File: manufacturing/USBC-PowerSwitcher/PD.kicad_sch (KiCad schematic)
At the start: 23 parts, among them J1 USB_C_Receptacle, J3 VDC, Q1 2N7002K, U2 CYPD3177-24LQXQ

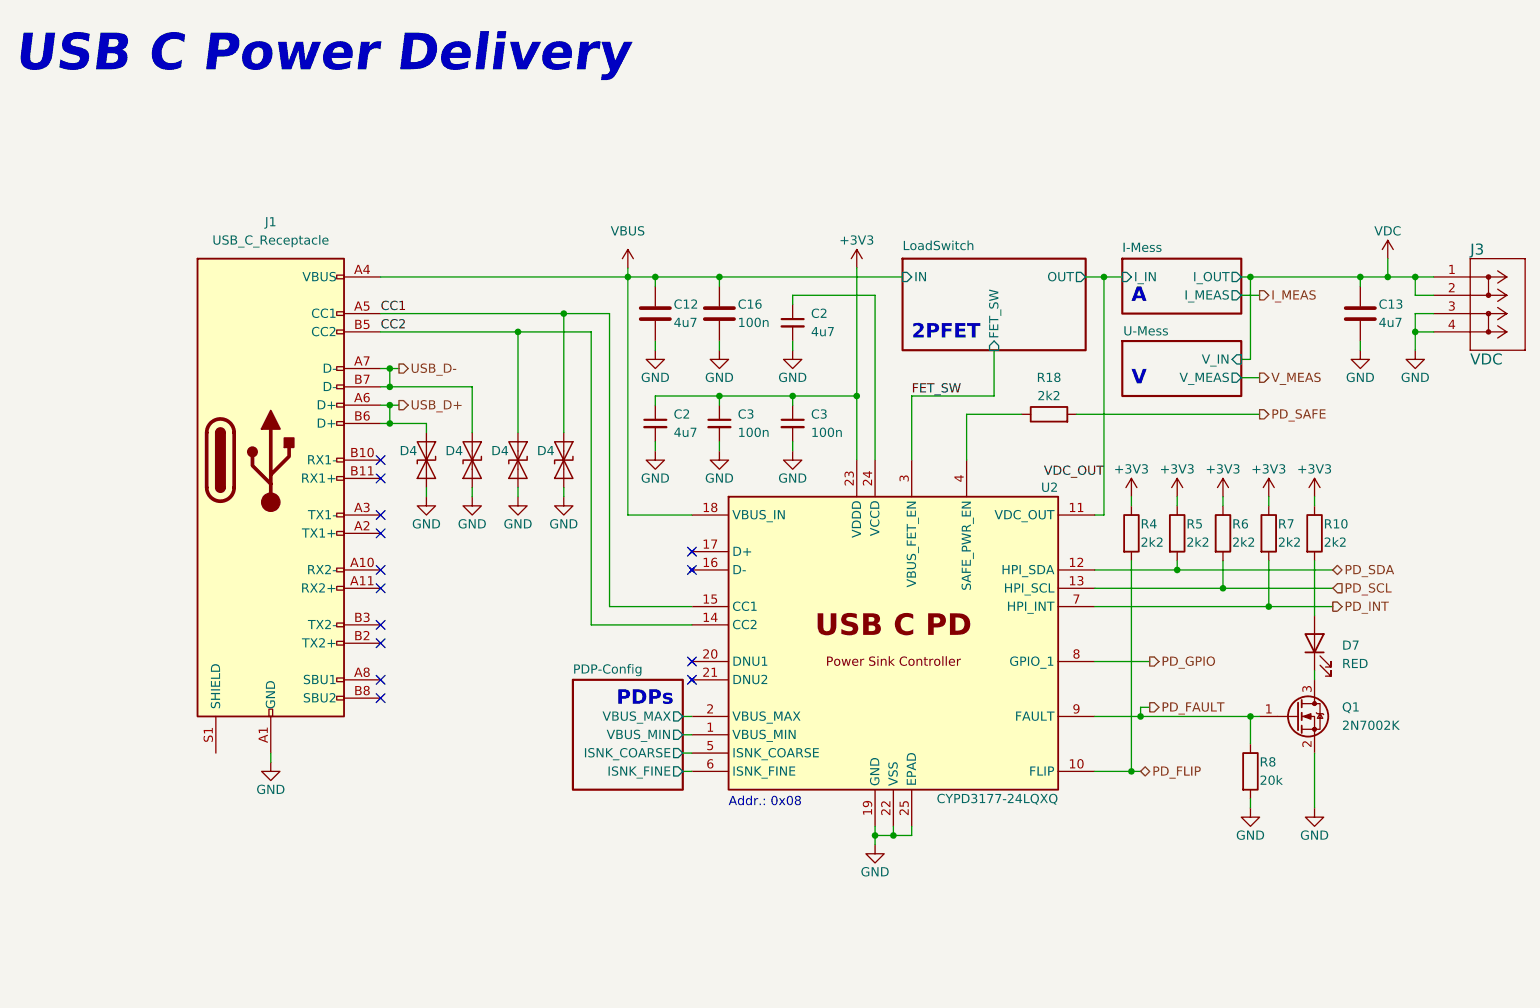
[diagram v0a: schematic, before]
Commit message: First Rough placement
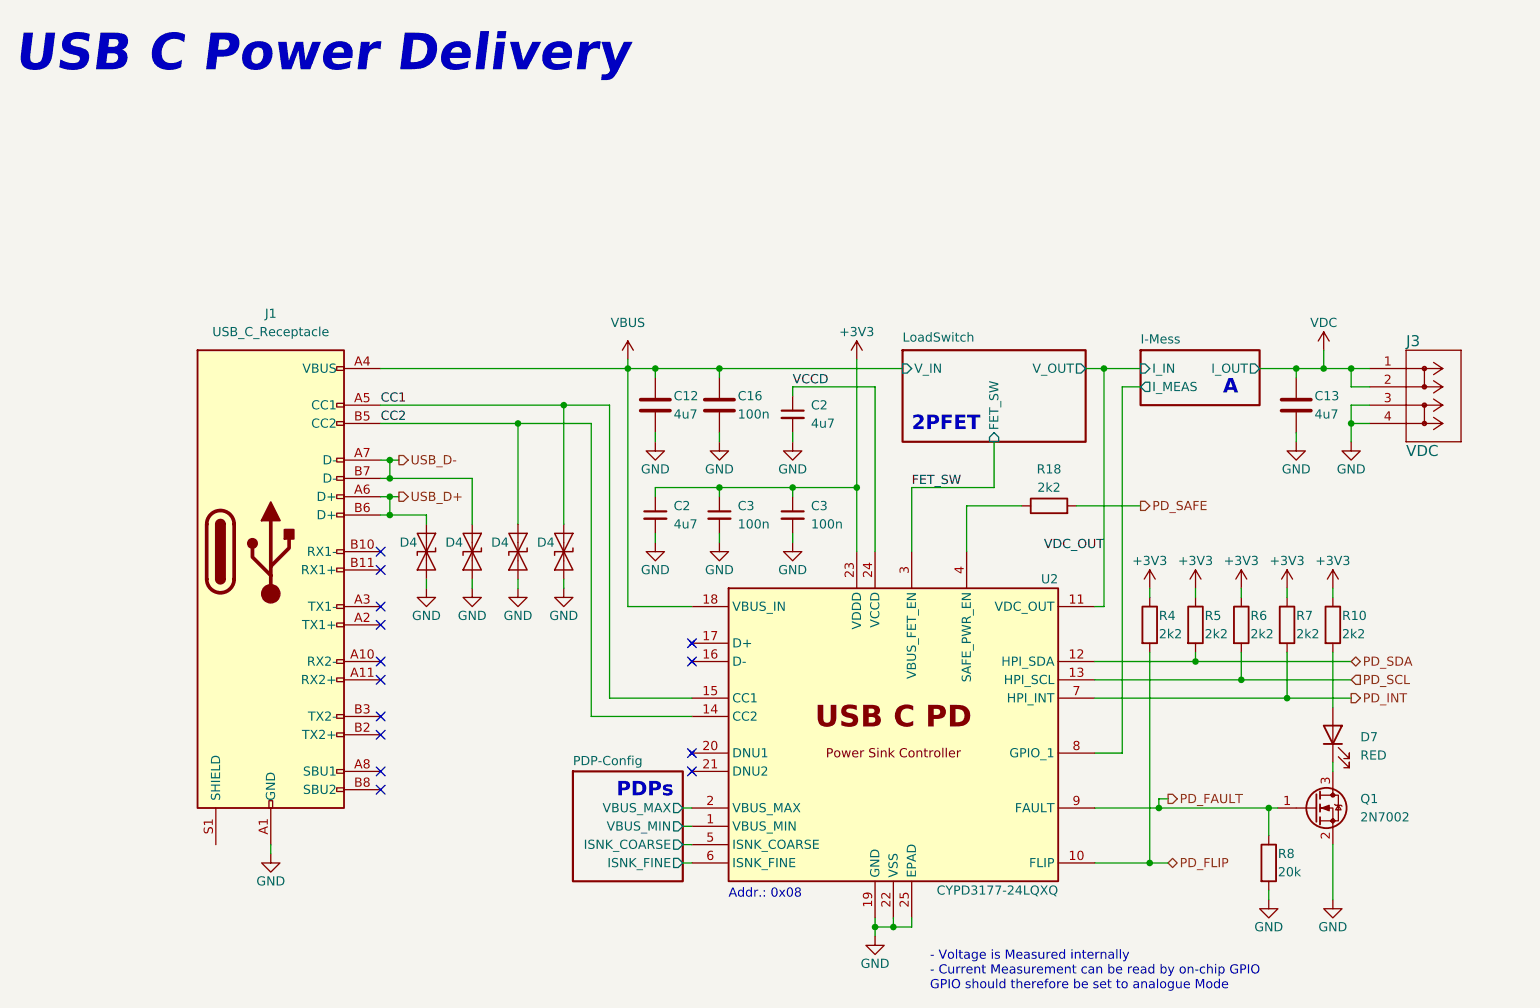
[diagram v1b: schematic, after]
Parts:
- C12, C13, C2: footprint (none) -> Capacitor_SMD:C_0805_2012Metric; LCSC # (none) -> C1779
- C16, C3: footprint (none) -> Capacitor_SMD:C_0402_1005Metric; LCSC # (none) -> C307331
- D4: LCSC # (none) -> C96512
- D7: footprint (none) -> LED_SMD:LED_0805_2012Metric; LCSC # (none) -> C84256
- J1: footprint (none) -> Connector_USB:USB_C_Receptacle_Molex_105450-0101; LCSC # (none) -> C134092
- J3: Reichelt # (none) -> WAGO 2604-1102
- Q1: value 2N7002K -> 2N7002; LCSC # (none) -> C8545
- R10, R18, R4, R5, R6, R7: footprint (none) -> Resistor_SMD:R_0402_1005Metric; LCSC # (none) -> C25879
- R8: footprint (none) -> Resistor_SMD:R_0402_1005Metric; LCSC # (none) -> C25765
- U2: LCSC # (none) -> C2959321
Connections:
- net VCCD: now reaches C2.1, U2.24 (VCCD)
- net PD_GPIO renamed I-Mess/I_MEAS
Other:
- removed sheet U-Mess
- sheet LoadSwitch ports: added V_IN, V_OUT; removed IN, OUT
- note added: "- Voltage is Measured internally - Current Measurement can be read by on-chip GPIO GPIO should therefore be set to analogue Mode"
- note removed: "V"
- moved on the sheet: C12, C13, C16, C2, C3, D4, D7, J1, J3, Q1, R10, R18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
